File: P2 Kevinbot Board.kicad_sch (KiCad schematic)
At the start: 33 parts, among them J11 Screw_Terminal_01x02, J13 Screw_Terminal_01x02, J14 Screw_Terminal_01x02, J2 Conn_02x06_Odd_Even, J20 Conn_02x06_Odd_Even, J23 Conn_02x06_Odd_Even, J24 Conn_01x04, J25 Conn_01x04, J26 Conn_01x04, J27 Conn_01x04, J29 Conn_01x02, J3 Screw_Terminal_01x02, J4 Conn_02x06_Odd_Even, J6 Conn_01x04_Male, J7 Conn_01x03_Male, SW1 SW_Push, U1 P2_EDGE_MODULE_SOCKET, U3 DS18B20

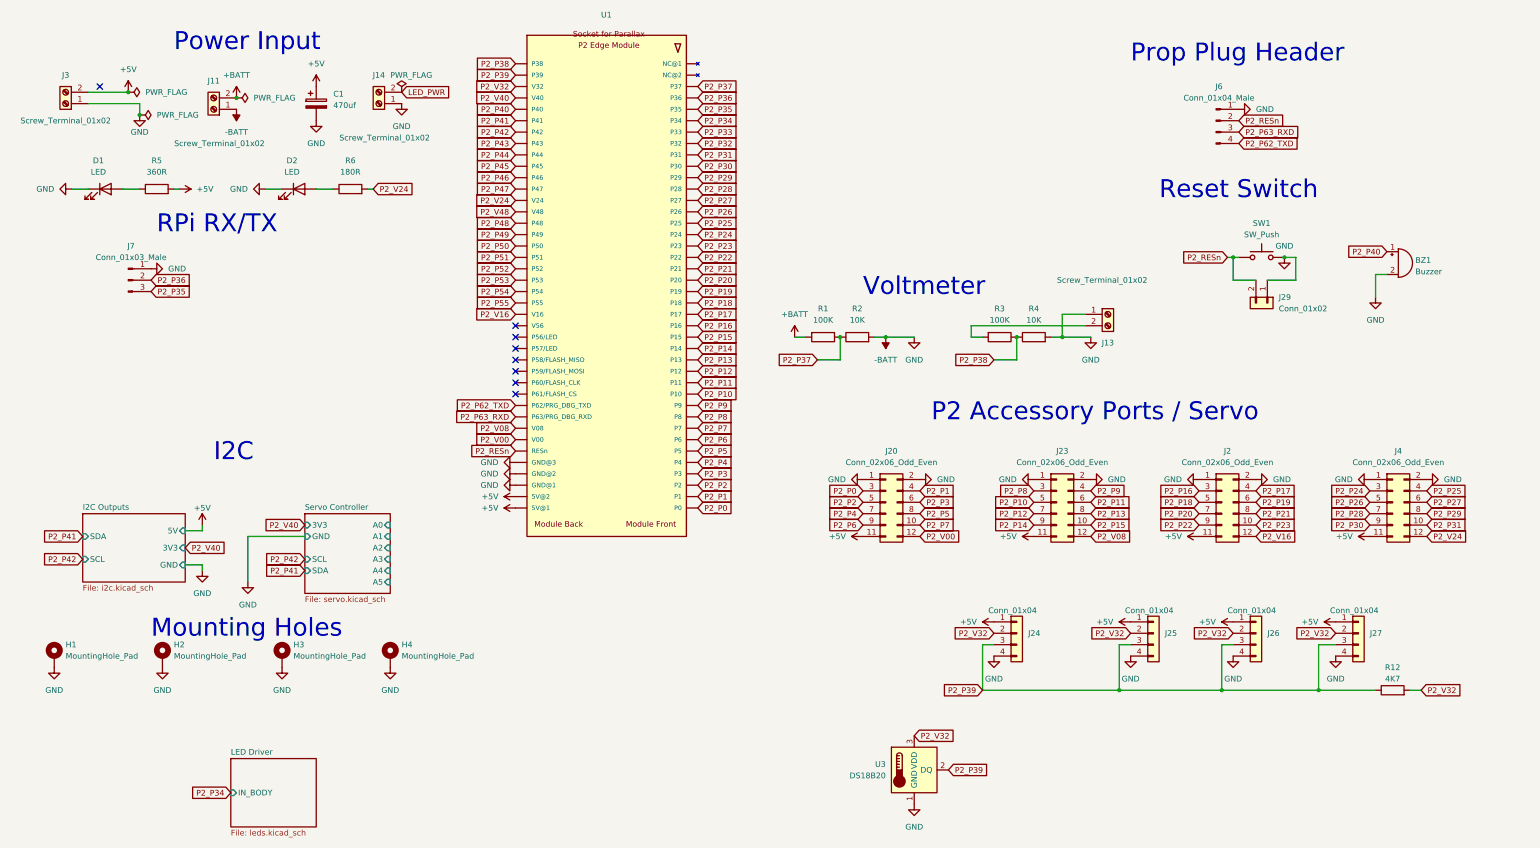
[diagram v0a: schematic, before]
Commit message: Fix global labels
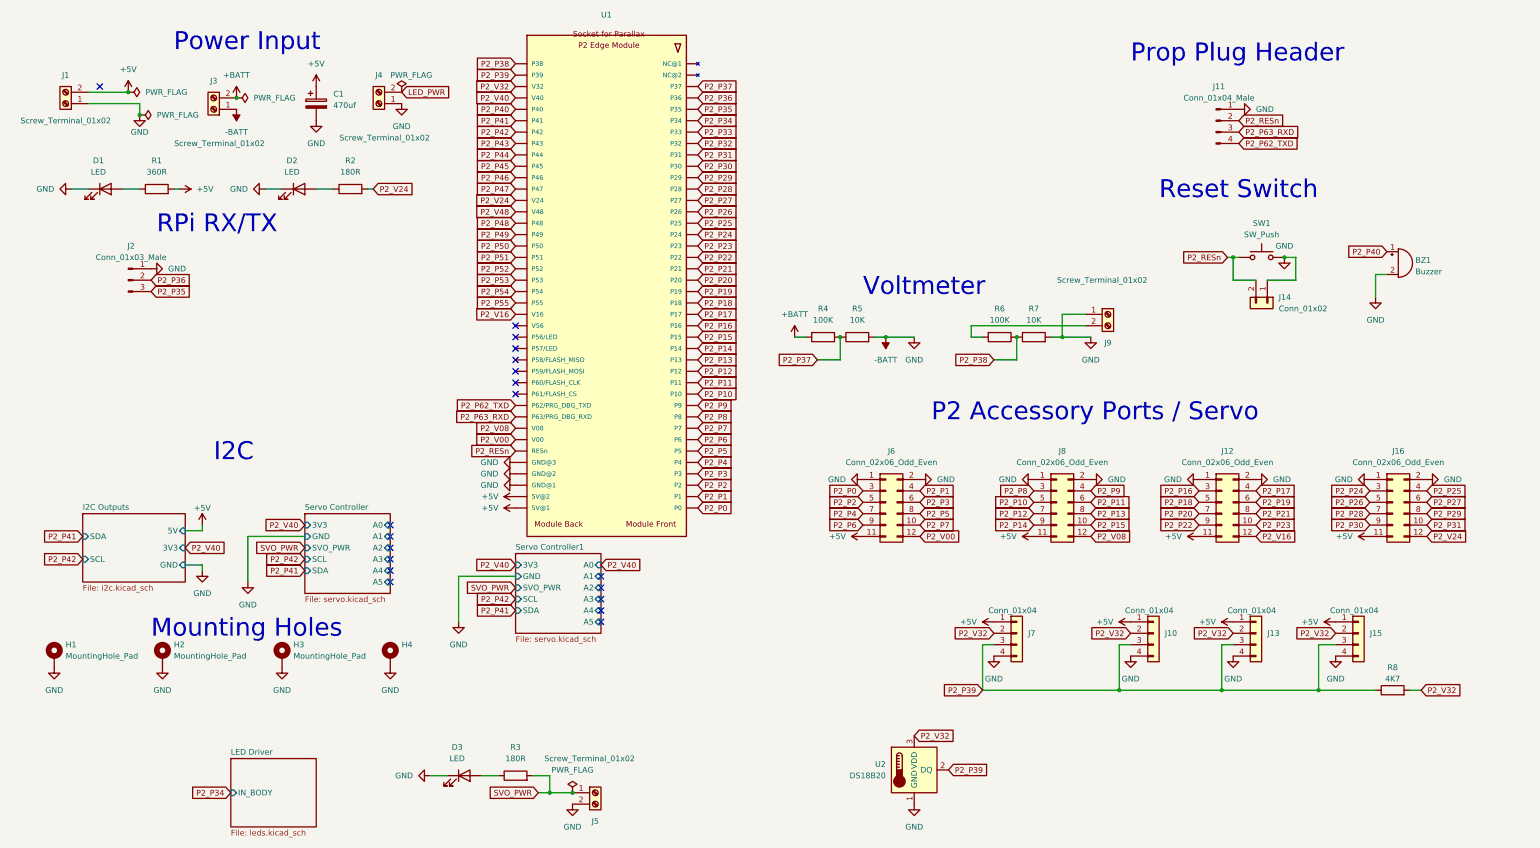
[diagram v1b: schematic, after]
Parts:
- added D3: LED, LED_SMD:LED_0805_2012Metric, symbol Device:LED
- added J5: Screw_Terminal_01x02, Phoenix_MSTBA:MSTBA-2,5-2-G-5,08, symbol Connector:Screw_Terminal_01x02
- added R3: 180R, Resistor_SMD:R_0805_2012Metric, symbol Device:R
- renumbered J3 to J1, J25 to J10, J6 to J11, J2 to J12, J26 to J13, J29 to J14, J27 to J15, J4 to J16, J7 to J2, J11 to J3, J14 to J4, J20 to J6, J24 to J7, J23 to J8, J13 to J9, R5 to R1, R6 to R2, R1 to R4, R2 to R5, R3 to R6, R4 to R7, R12 to R8, U3 to U2
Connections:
- net -BATT: now also D3.1 (K), J5.2 (Pin_2)
- new net: D3.2 (A), R3.1
- new net SVO_PWR: J5.1 (Pin_1), R3.2
- no-connect marks 8 -> 19
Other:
- added sheet Servo Controller1 (servo.kicad_sch)
- sheet Servo Controller ports: added SVO_PWR; removed none

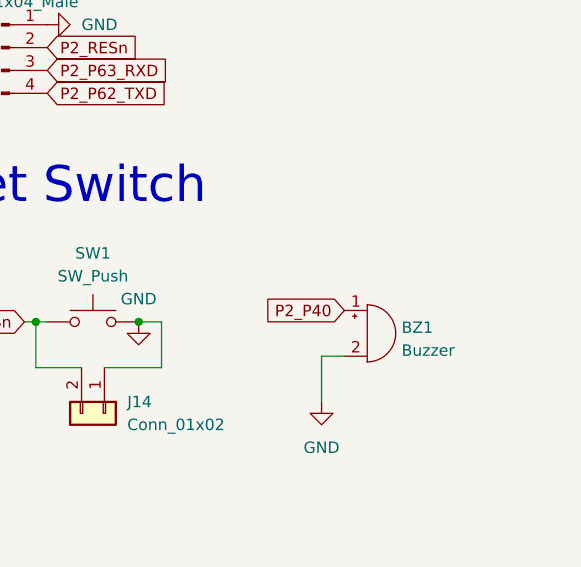
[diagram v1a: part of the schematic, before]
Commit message: Add int buzzer enable jumper
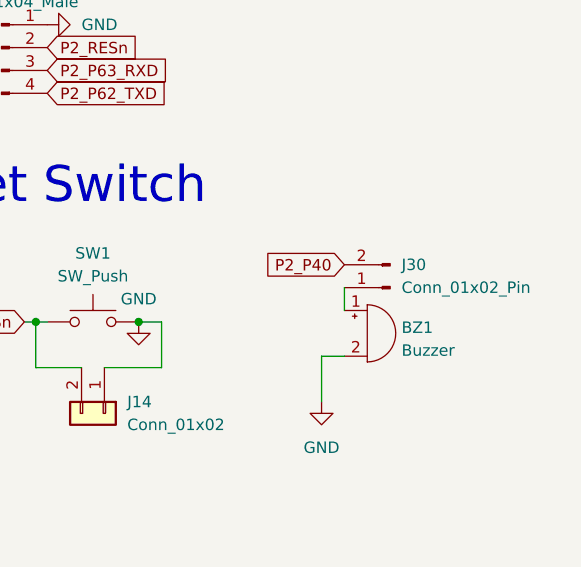
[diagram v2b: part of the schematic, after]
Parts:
- added J30: Conn_01x02_Pin, Connector_PinHeader_2.54mm:PinHeader_1x02_P2.54mm_Vertical, symbol Connector:Conn_01x02_Pin
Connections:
- net P2_P40: now also J30.2 (Pin_2); no longer BZ1.1 (-)
- new net: BZ1.1 (-), J30.1 (Pin_1)
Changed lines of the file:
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@@
 	(wire
 		(pts
+			(xy 320.04 66.04) (xy 320.04 68.58)
+		)
+		(stroke
+			(width 0)
+			(type default)
+		)
+	)
+	(wire
+		(pts
 			(xy 247.65 82.55) (xy 247.65 87.63)
 		)
@@
 	(global_label "P2_P40"
 		(shape input)
-		(at 320.04 68.58 180)
+		(at 320.04 63.5 180)
 		(fields_autoplaced yes)
 		(effects
@@
 		)
 		(property "Intersheetrefs" "${INTERSHEET_REFS}"
-			(at 309.9981 68.58 0)
+			(at 309.9981 63.5 0)
 			(effects
 				(font
@@
 					(unit 1)
 				)
+			)
+		)
+	)
+	(symbol
+		(lib_id "Connector:Conn_01x02_Pin")
+		(at 325.12 66.04 180)
+		(unit 1)
+		(exclude_from_sim no)
+		(in_bom yes)
+		(on_board yes)
+		(dnp no)
+		(fields_autoplaced yes)
+		(property "Reference" "J30"
+			(at 326.39 63.4999 0)
+			(effects
+				(font
+					(size 1.27 1.27)
+				)
+				(justify right)
+			)
+		)
+		(property "Value" "Conn_01x02_Pin"
+			(at 326.39 66.0399 0)
+			(effects
+				(font
+					(size 1.27 1.27)
+				)
+				(justify right)
+			)
+		)
+		(property "Footprint" "Connector_PinHeader_2.54mm:PinHeader_1x02_P2.54mm_Vertical"
+			(at 325.12 66.04 0)
+			(effects
+				(font
+					(size 1.27 1.27)
+				)
+				(hide yes)
+			)
+		)
+		(property "Datasheet" "~"
+			(at 325.12 66.04 0)
+			(effects
+				(font
+					(size 1.27 1.27)
+				)
+				(hide yes)
+			)
+		)
+		(property "Description" "Generic connector, single row, 01x02, script generated"
+			(at 325.12 66.04 0)
+			(effects
+				(font
+					(size 1.27 1.27)
+				)
+				(hide yes)
+			)
+		)
+		(pin "2"
+		)
+		(pin "1"
+		)
+		(instances
+			(project ""
+				(path "/362ca48c-0b77-4943-b8b3-fc15ab97f30d"
+					(reference "J30")
+					(unit 1)
+				)

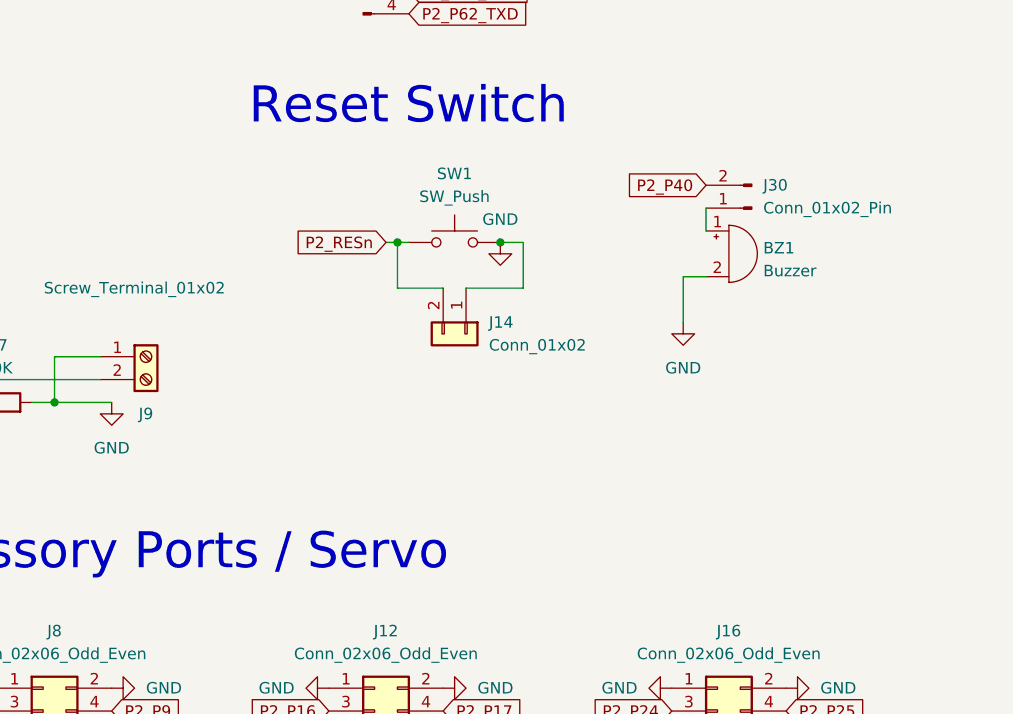
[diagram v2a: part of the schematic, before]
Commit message: Add ext buzzer fet and connector
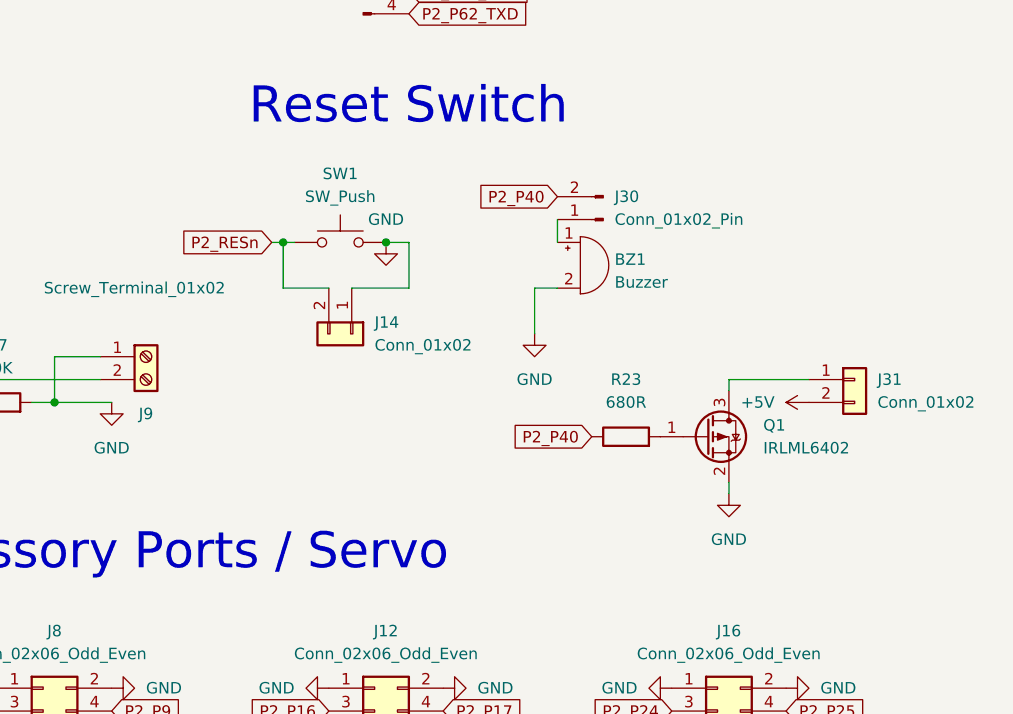
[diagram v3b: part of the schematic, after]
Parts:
- added J31: Conn_01x02, Connector_JST:JST_XH_B2B-XH-A_1x02_P2.50mm_Vertical, symbol Connector_Generic:Conn_01x02
- added Q1: IRLML6402, Package_TO_SOT_SMD:SOT-23, symbol Transistor_FET:IRLML6402
- added R23: 680R, Resistor_SMD:R_0603_1608Metric, symbol Device:R
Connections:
- net +5V: now also J31.2 (Pin_2)
- net -BATT: now also Q1.2 (S)
- net P2_P40: now also R23.1
- new net: J31.1 (Pin_1), Q1.3 (D)
- new net: Q1.1 (G), R23.2
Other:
- moved on the sheet: BZ1, J14, J30, SW1
